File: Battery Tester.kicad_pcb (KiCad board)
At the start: 2 copper layers, 97 x 157 mm, 184 parts, among them J1 USB-C Receptacle, J2 JST-PH, J3 FTS-107-01-X-DV-A, J5 OLED DISPLAY, J6 FLE-105-01-X-DV-A, J7 TFM-110-12-X-D-A, J8 JST-PH, Q1 IRF540N, Q2 IRF540N, SW1 Reset, SW2 BOOTSEL, SW3 RotaryEncoder_Switch, SW4 Start/Stop, SW5 Charge, SW6 Discharge, U1 RP2040, U10 TLV9001IDCK, U11 MCP4725xxx-xCH, U12 MCP4725xxx-xCH, U13 MCP4725xxx-xCH, U14 TLV9001IDCK, U15 TLV9001IDCK, U16 INA219BxD, U17 MAX17048G, U2 W25Q32JVSS, U3 USBLC6-2SC6, U4 AP2112K-3.3, U5 MAX17048G, U6 LTC4001, U7 INA219BxD, U8 TLV9001IDCK, U9 MCP4725xxx-xCH, Y1 12MHz

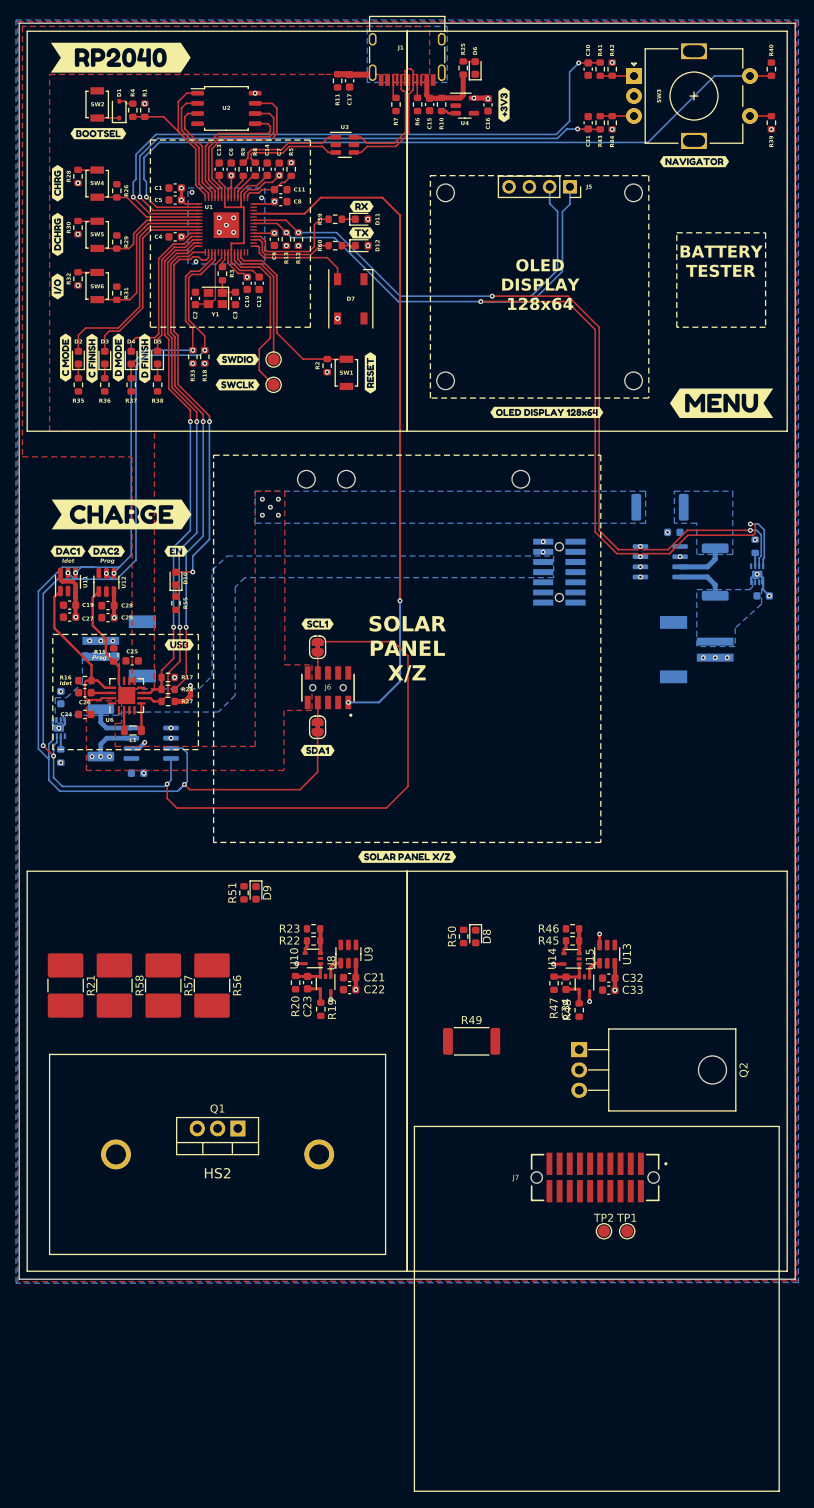
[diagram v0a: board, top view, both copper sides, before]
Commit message: Finished Routing
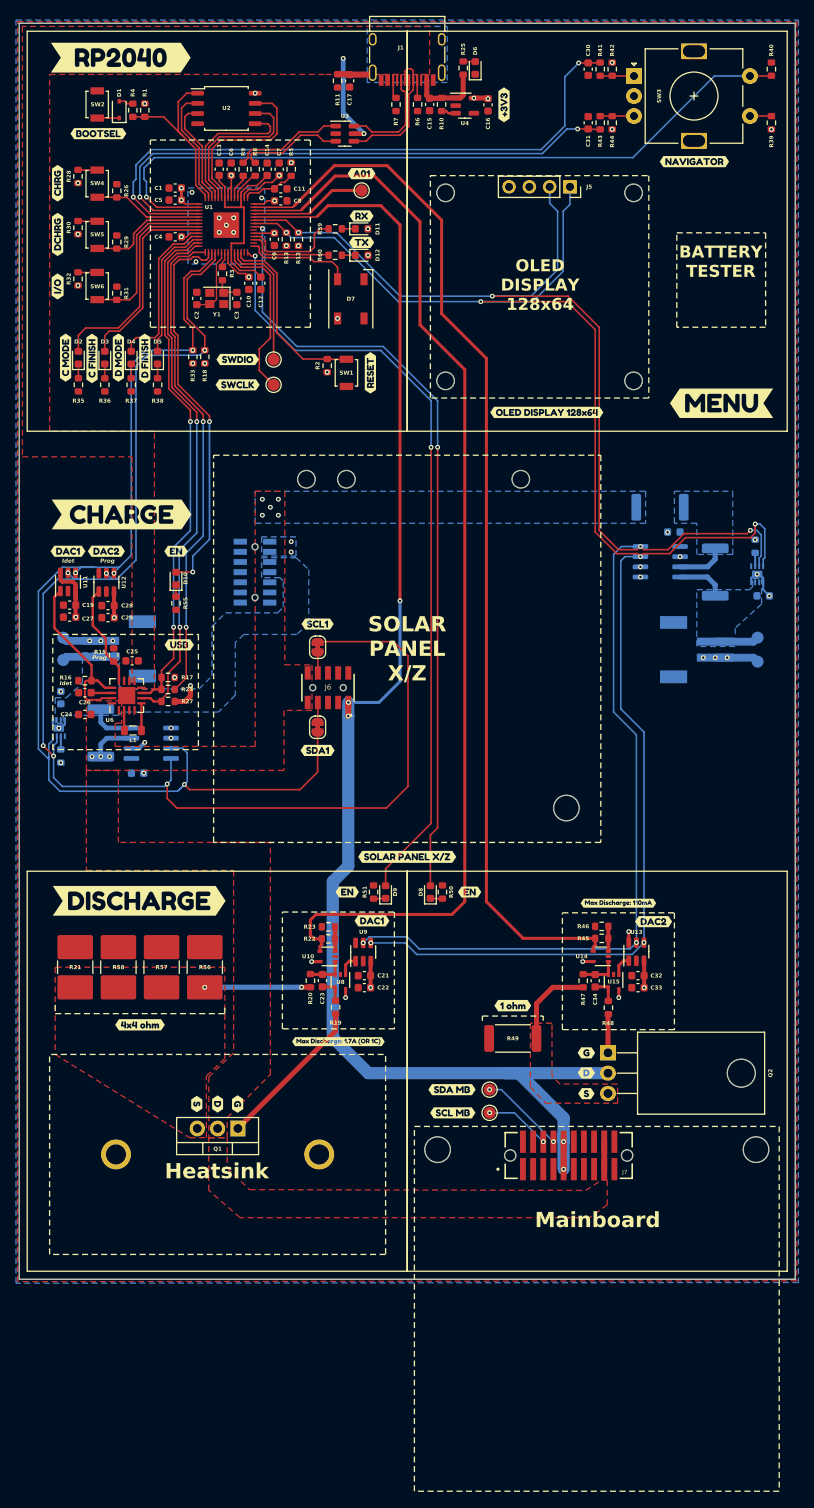
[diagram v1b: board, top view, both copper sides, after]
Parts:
- added REF**: MountingHole_3.2mm_M3_DIN965, MountingHole:MountingHole_3.2mm_M3_DIN965, F.Cu at (113.0, 124.4)
- added REF**: MountingHole_3.2mm_M3_DIN965, MountingHole:MountingHole_3.2mm_M3_DIN965, F.Cu at (96.9, 167.1)
- added REF**: MountingHole_3.2mm_M3_DIN965, MountingHole:MountingHole_3.2mm_M3_DIN965, F.Cu at (136.7, 167.1)
- added TP5: A01, TestPoint:TestPoint_Pad_D1.5mm, F.Cu at (87.4, 47.2)
- added TP6: BATT_SENS, TestPoint:TestPoint_Pad_D1.5mm, B.Cu at (50.1, 105.9)
- added TP7: GND, TestPoint:TestPoint_Pad_D1.5mm, B.Cu at (50.1, 103.1)
- added TP8: BATT_SENS_2, TestPoint:TestPoint_Pad_D1.5mm, B.Cu at (136.9, 103.1)
- added TP9: GND, TestPoint:TestPoint_Pad_D1.5mm, B.Cu at (136.9, 106.1)
- added kibuzzard-643A0700: G***, kibuzzard-643A0700, F.Cu at (88.7, 138.5)
- added kibuzzard-643A09FA: G***, kibuzzard-643A09FA, F.Cu at (100.9, 134.9)
- added kibuzzard-643A09FA: G***, kibuzzard-643A09FA, F.Cu at (85.6, 134.9)
- added kibuzzard-643CBBC0: G***, kibuzzard-643CBBC0, F.Cu at (87.4, 45.1)
- added kibuzzard-6445C5A7: G***, kibuzzard-6445C5A7, F.Cu at (59.6, 136.0)
- added kibuzzard-6445C801: G***, kibuzzard-6445C801, F.Cu at (84.5, 153.6)
- added kibuzzard-6445C9CC: G***, kibuzzard-6445C9CC, F.Cu at (59.7, 151.5)
- added kibuzzard-6445CB82: G***, kibuzzard-6445CB82, F.Cu at (123.9, 138.6)
- added kibuzzard-6445CBB2: G***, kibuzzard-6445CBB2, F.Cu at (98.7, 159.6)
- added kibuzzard-6445CBC6: G***, kibuzzard-6445CBC6, F.Cu at (98.8, 162.5)
- added kibuzzard-6445CBEB: G***, kibuzzard-6445CBEB, F.Cu at (119.5, 136.3)
- added kibuzzard-6445CC26: G***, kibuzzard-6445CC26, F.Cu at (106.3, 149.1)
- added kibuzzard-6445CC4D: G***, kibuzzard-6445CC4D, F.Cu at (115.5, 155.0)
- added kibuzzard-6445CC4D: G***, kibuzzard-6445CC4D, F.Cu at (71.9, 161.4)
- added kibuzzard-6445CCAB: G***, kibuzzard-6445CCAB, F.Cu at (115.5, 157.5)
- added kibuzzard-6445CCAB: G***, kibuzzard-6445CCAB, F.Cu at (69.4, 161.4)
- added kibuzzard-6445CCB6: G***, kibuzzard-6445CCB6, F.Cu at (66.8, 161.4)
- added kibuzzard-6445CCB6: G***, kibuzzard-6445CCB6, F.Cu at (115.5, 160.1)
- added kibuzzard-6445CDE6: G***, kibuzzard-6445CDE6, B.Cu at (128.9, 112.8)
- added kibuzzard-6445CE6B: G***, kibuzzard-6445CE6B, B.Cu at (50.1, 101.0)
- added kibuzzard-6445CE94: G***, kibuzzard-6445CE94, B.Cu at (50.1, 108.0)
- added kibuzzard-6445CEE7: G***, kibuzzard-6445CEE7, B.Cu at (63.0, 104.5)
- added kibuzzard-6445CEE7: G***, kibuzzard-6445CEE7, B.Cu at (123.2, 104.6)
- added kibuzzard-6445CF1E: G***, kibuzzard-6445CF1E, B.Cu at (46.0, 114.4)
- added kibuzzard-6445CF1E: G***, kibuzzard-6445CF1E, B.Cu at (140.1, 95.2)
- added kibuzzard-6445CFA2: G***, kibuzzard-6445CFA2, B.Cu at (59.4, 123.9)
- added kibuzzard-6445CFCB: G***, kibuzzard-6445CFCB, B.Cu at (54.9, 120.0)
- added kibuzzard-6445D503: G***, kibuzzard-6445D503, B.Cu at (131.6, 90.1)
- added kibuzzard-6445D545: G***, kibuzzard-6445D545, B.Cu at (124.7, 82.4)
- added kibuzzard-6445D55B: G***, kibuzzard-6445D55B, B.Cu at (124.7, 83.9)
- J3: value FTS-107-01-X-DV-A -> FLE-107-01-X-DV-A; footprint BatteryTester:SAMTEC-FTS-107-01-X-DV-A -> BatteryTester:SAMTEC_FLE-107-01-X-DV-A
- moved J3 38.0 mm to (74.1, 94.9)
- moved TP2 22.8 mm to (103.4, 159.6)
- moved TP1 22.7 mm to (103.4, 162.5)
- moved D9 16.2 mm to (90.4, 134.9), turned to 90 degrees
- moved R51 16.2 mm to (88.9, 134.9), turned to -90 degrees
- moved D8 7.93 mm to (96.0, 134.9), turned to 90 degrees
- moved R50 6.16 mm to (97.5, 134.9), turned to -90 degrees
- moved R49 5.16 mm to (106.3, 153.2)
- moved J7 4.31 mm to (113.3, 167.8), turned to 0 degrees
- moved R48 3.66 mm to (118.2, 149.3)
- moved U13 3.66 mm to (121.7, 142.4)
- moved U15 3.66 mm to (118.9, 146.2)
- moved C32 3.66 mm to (121.9, 145.4)
- moved C33 3.66 mm to (121.9, 146.9)
- moved C34 3.66 mm to (116.6, 146.0)
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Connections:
- D8 pad 2: unconnected-(D8-A-Pad2) -> /D15
- D9 pad 2: unconnected-(D9-A-Pad2) -> /D14
- HS2 pad 2: (no net) -> GND
- R22 pad 1: /A00 -> /A02
- U1 pad 28: /USB_HOSTEN -> /D14
- U1 pad 35: unconnected-(U1-GPIO23-Pad35) -> /D15
- U1 pad 38: /A00 -> 3V3_SP
- U1 pad 39: 3V3_SP -> /A01
- U10 pad 4: /A00 -> /A02
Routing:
- net /A02: track 0.00 -> 137.7 mm
- net /A03: track 1.70 -> 133.2 mm
- net 3V3_SP: track 85.9 -> 185.4 mm, vias 2 -> 5
- net /D15: track 0.00 -> 99.1 mm, vias 0 -> 2
- net /D14: track 0.00 -> 97.6 mm, vias 0 -> 2
- net /SCL0: track 121.3 -> 210.1 mm, vias 4 -> 6
- net /SDA0: track 127.0 -> 213.1 mm, vias 4 -> 6
- net Net-(Q1-G): track 0.00 -> 19.4 mm
- net /A01: track 0.00 -> 14.7 mm
- net Net-(Q1-S): track 0.00 -> 13.2 mm, vias 0 -> 2
- net VBUS: track 9.36 -> 21.1 mm, vias 0 -> 2
- net Net-(Q2-S): track 0.00 -> 11.0 mm
- net Net-(J7-Pin_8): track 0.00 -> 10.7 mm, vias 0 -> 2
- net GND: track 9.95 -> 20.3 mm
- net Net-(J7-Pin_6): track 0.00 -> 8.21 mm, vias 0 -> 2
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- added copper zone on F.Cu, net Net-(Q1-S)
- added copper zone on F.Cu, net Net-(Q2-S)
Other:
- board text added: "Heatsink"
- board text added: "MIDDLE BATTERY BOARD"
- board text added: "Mainboard"
